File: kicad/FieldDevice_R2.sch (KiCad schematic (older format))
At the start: 0 parts

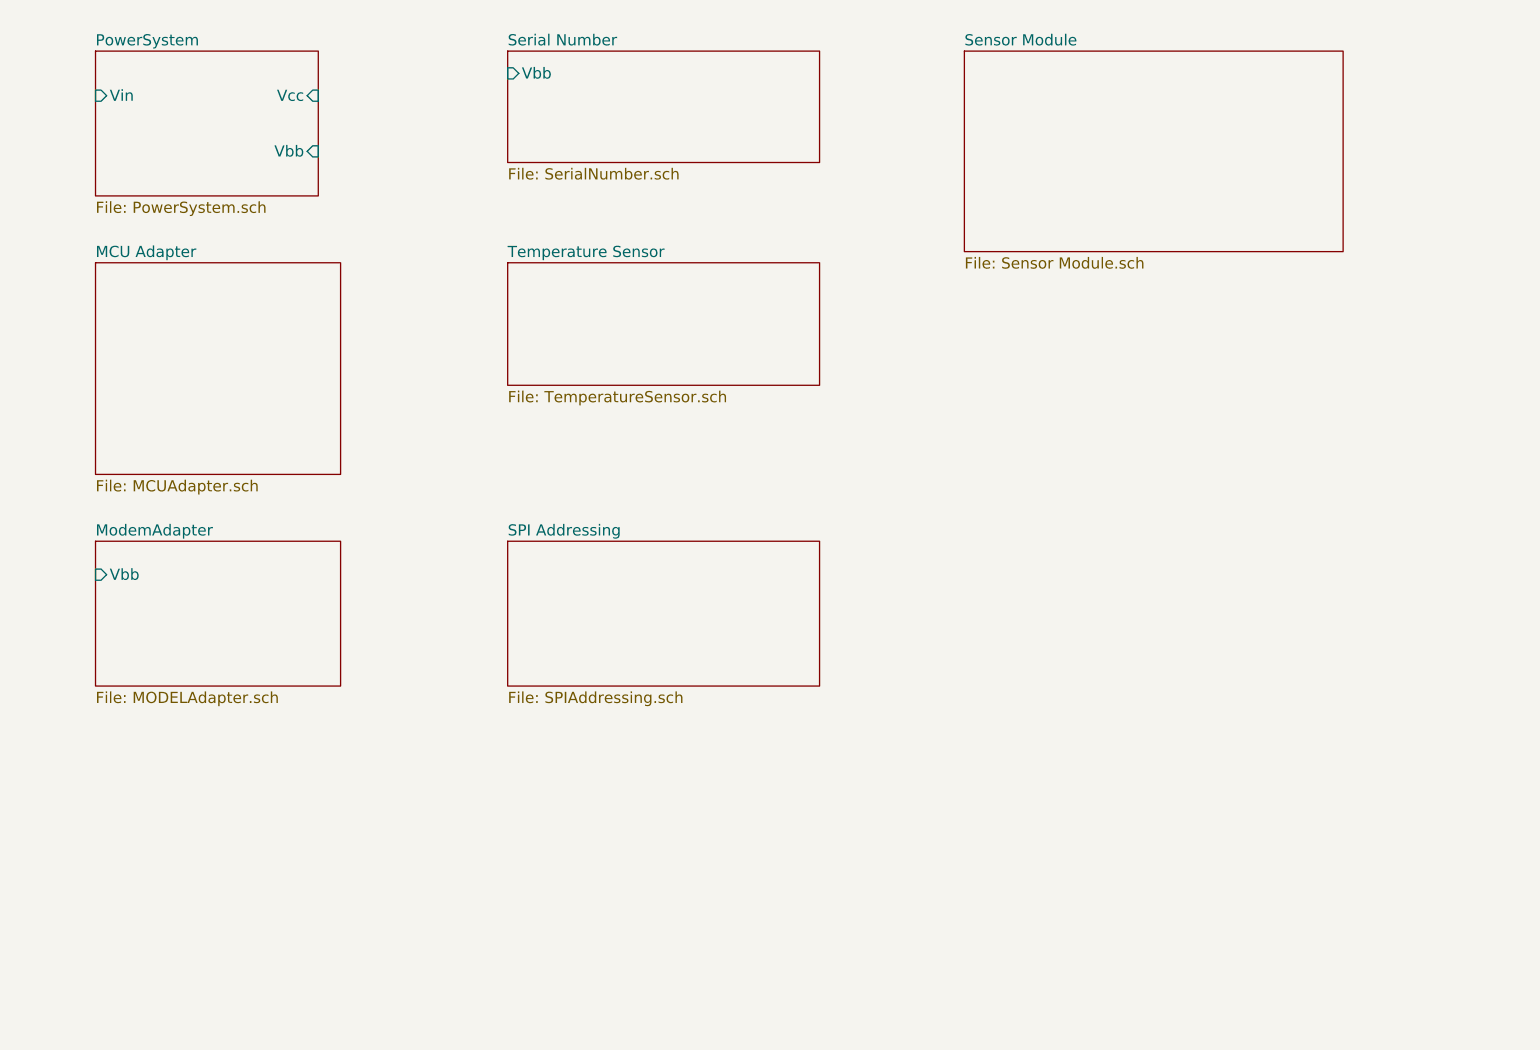
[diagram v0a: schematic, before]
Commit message: First draft of some of the sub-sheets
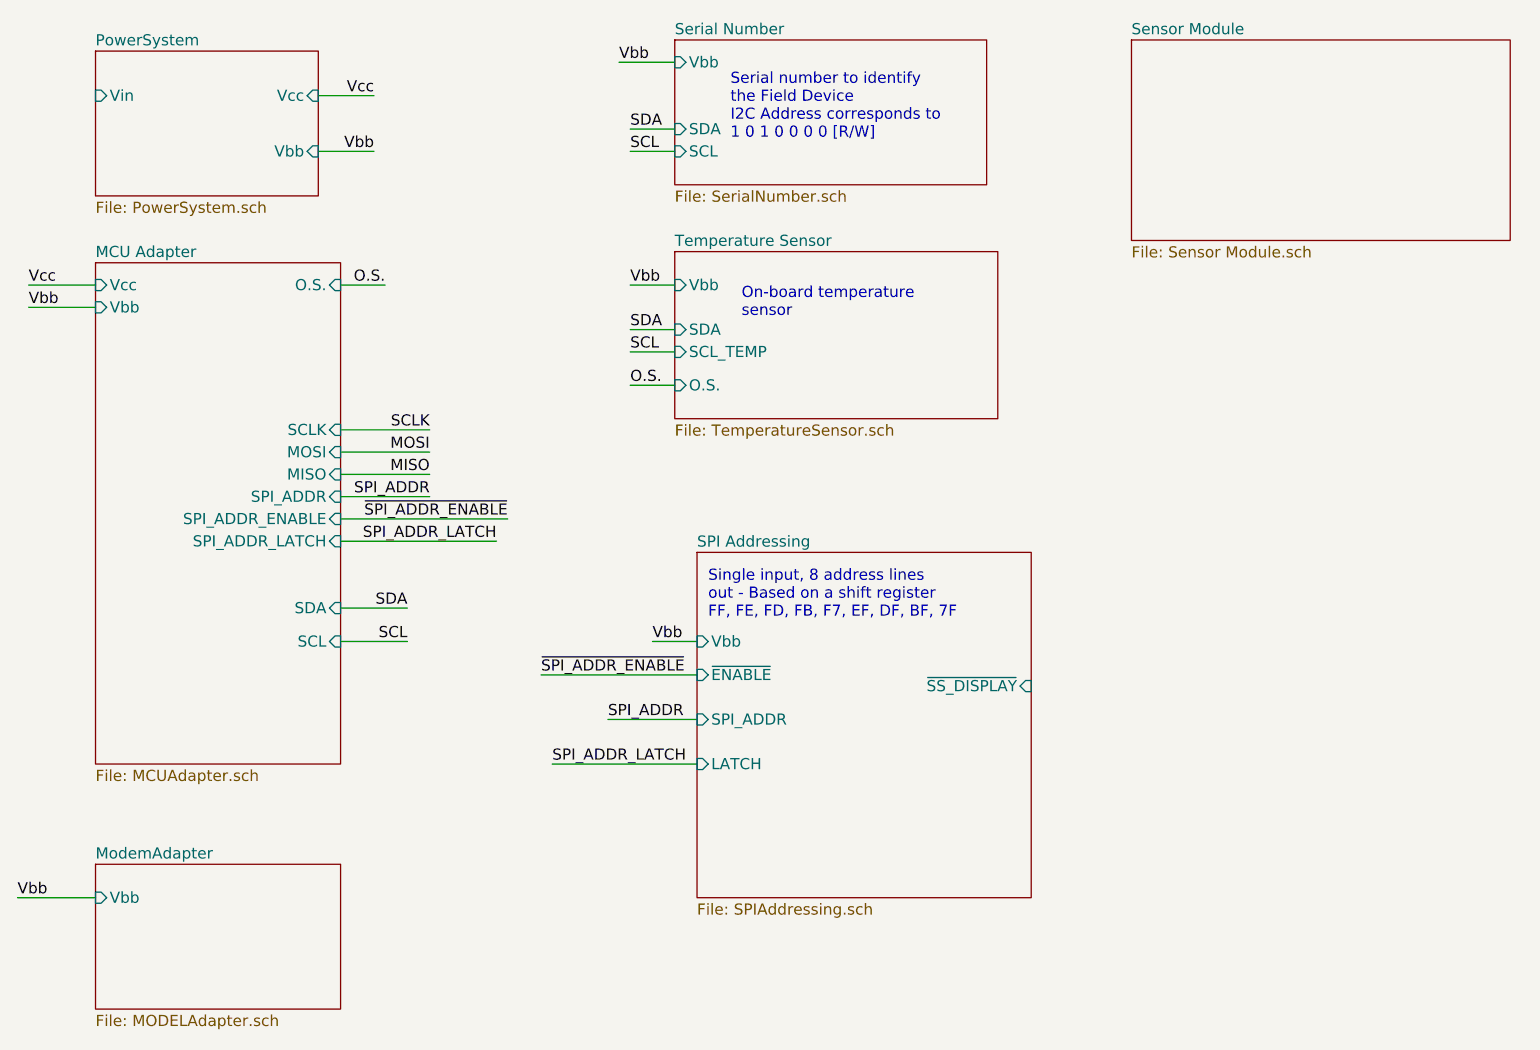
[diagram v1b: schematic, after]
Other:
- note added: "On-board temperature \nsensor"
- note added: "Serial number to identify \nthe Field Device\nI2C Address corresponds to \n1 0 1 0 0 0 0 [R/W]"
- note added: "Single input, 8 address lines \nout - Based on a shift register\nFF, FE, FD, FB, F7, EF, DF, BF, 7F"
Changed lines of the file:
@@
 EESchema Schematic File Version 4
 LIBS:FieldDevice_R2-cache
+LIBS:FieldDevice_Power_5V-cache
 EELAYER 26 0
 EELAYER END
@@
 $EndSheet
 $Sheet
-S 3450 3100 1400 650
-U 5C1FCC69
-F0 "SPI Addressing" 50
-F1 "SPIAddressing.sch" 50
-$EndSheet
-$Sheet
-S 3450 900  1400 500
+S 4200 850  1400 650
 U 5C1FCC6C
 F0 "Serial Number" 50
 F1 "SerialNumber.sch" 50
-F2 "Vbb" I L 3450 1000 50
+F2 "Vbb" I L 4200 950 50
+F3 "SDA" I L 4200 1250 50
+F4 "SCL" I L 4200 1350 50
 $EndSheet
 $Sheet
-S 3450 1850 1400 550
+S 4200 1800 1450 750
 U 5C1FCC6F
 F0 "Temperature Sensor" 50
 F1 "TemperatureSensor.sch" 50
+F2 "O.S." I L 4200 2400 50
+F3 "SCL_TEMP" I L 4200 2250 50
+F4 "SDA" I L 4200 2150 50
+F5 "Vbb" I L 4200 1950 50
 $EndSheet
 $Sheet
-S 5500 900  1700 900
+S 6250 850  1700 900
 U 5C1FCC72
 F0 "Sensor Module" 50
@@
 $EndSheet
 $Sheet
-S 1600 1850 1100 950
+S 1600 1850 1100 2250
 U 5C1FCC75
 F0 "MCU Adapter" 50
 F1 "MCUAdapter.sch" 50
+F2 "Vcc" I L 1600 1950 50
+F3 "Vbb" I L 1600 2050 50
+F4 "SDA" I R 2700 3400 50
+F5 "SCL" I R 2700 3550 50
+F6 "O.S." I R 2700 1950 50
+F7 "SPI_ADDR" I R 2700 2900 50
+F8 "SCLK" I R 2700 2600 50
+F9 "MOSI" I R 2700 2700 50
+F10 "MISO" I R 2700 2800 50
+F11 "SPI_ADDR_ENABLE" I R 2700 3000 50
+F12 "SPI_ADDR_LATCH" I R 2700 3100 50
 $EndSheet
 $Sheet
-S 1600 3100 1100 650
+S 1600 4550 1100 650
 U 5C1FCC78
 F0 "ModemAdapter" 50
 F1 "MODELAdapter.sch" 50
-F2 "Vbb" I L 1600 3250 50
+F2 "Vbb" I L 1600 4700 50
 $EndSheet
+Text Notes 4350 3450 0    50   ~ 0
+Single input, 8 address lines \nout - Based on a shift register\nFF, FE, FD, FB, F7, EF, DF, BF, 7F
+Text Notes 4450 1300 0    50   ~ 0
+Serial number to identify \nthe Field Device\nI2C Address corresponds to \n1 0 1 0 0 0 0 [R/W]
+Text Notes 4500 2100 0    50   ~ 0
+On-board temperature \nsensor
+Wire Wire Line
+	2600 1350 2850 1350
+Text Label 2850 1350 2    50   ~ 0
+Vbb
+Wire Wire Line
+	4200 950  3950 950
+Text Label 3950 950  0    50   ~ 0
+Vbb
+Wire Wire Line
+	4200 1950 4000 1950
+Text Label 4000 1950 0    50   ~ 0
+Vbb
+Wire Wire Line
+	2700 3550 3000 3550
+Wire Wire Line
+	2700 3400 3000 3400
+Text Label 3000 3400 2    50   ~ 0
+SDA
+Wire Wire Line
+	4200 2150 4000 2150
+Text Label 4000 2150 0    50   ~ 0
+SDA
+Wire Wire Line
+	4200 2250 4000 2250
+Text Label 4000 2250 0    50   ~ 0
+SCL
+Wire Wire Line
+	4200 2400 4000 2400
+Text Label 4000 2400 0    50   ~ 0
+O.S.
+Wire Wire Line
+	2700 1950 2900 1950
+Text Label 2900 1950 2    50   ~ 0
+O.S.
+Wire Wire Line
+	2600 1100 2850 1100
+Text Label 2850 1100 2    50   ~ 0
+Vcc
+Wire Wire Line
+	1600 1950 1300 1950
+Wire Wire Line
+	1600 2050 1300 2050
+Text Label 1300 1950 0    50   ~ 0
+Vcc
+Text Label 1300 2050 0    50   ~ 0
+Vbb
+Wire Wire Line
+	1600 4700 1250 4700
+Text Label 1250 4700 0    50   ~ 0
+Vbb
+Wire Wire Line
+	4300 3550 4100 3550
+Text Label 4100 3550 0    50   ~ 0
+Vbb
+Wire Wire Line
+	4200 1250 4000 1250
+Wire Wire Line
+	4200 1350 4000 1350
+Text Label 3000 3550 2    50   ~ 0
+SCL
+$Sheet
+S 4300 3150 1500 1550
+U 5C1FCC69
+F0 "SPI Addressing" 50
+F1 "SPIAddressing.sch" 50
+F2 "Vbb" I L 4300 3550 50
+F3 "SPI_ADDR" I L 4300 3900 50
+F4 "~SS_DISPLAY" I R 5800 3750 50
+F5 "LATCH" I L 4300 4100 50
+F6 "~ENABLE" I L 4300 3700 50
+$EndSheet
+Text Label 4000 1250 0    50   ~ 0
+SDA
+Text Label 4000 1350 0    50   ~ 0
+SCL
+Text Label 3900 3900 0    50   ~ 0
+SPI_ADDR
+Wire Wire Line
+	4300 3900 3900 3900
+Wire Wire Line
+	2700 2900 3100 2900
+Text Label 3100 2900 2    50   ~ 0
+SPI_ADDR
+Wire Wire Line
+	2700 2800 3100 2800
+Wire Wire Line
+	2700 2700 3100 2700
+Wire Wire Line
+	2700 2600 3100 2600
+Text Label 3100 2600 2    50   ~ 0
+SCLK
+Text Label 3100 2700 2    50   ~ 0
+MOSI
+Text Label 3100 2800 2    50   ~ 0
+MISO
+Text Label 3600 3700 0    50   ~ 0
+~SPI_ADDR_ENABLE
+Wire Wire Line
+	4300 3700 3600 3700
+Wire Wire Line
+	2700 3000 3450 3000
+Text Label 3450 3000 2    50   ~ 0
+~SPI_ADDR_ENABLE
+Text Label 3650 4100 0    50   ~ 0
+SPI_ADDR_LATCH
+Wire Wire Line
+	4300 4100 3650 4100
+Text Label 3400 3100 2    50   ~ 0
+SPI_ADDR_LATCH
+Wire Wire Line
+	2700 3100 3400 3100
 $EndSCHEMATC

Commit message: Added some more detail and moved the display from SPI to I2C
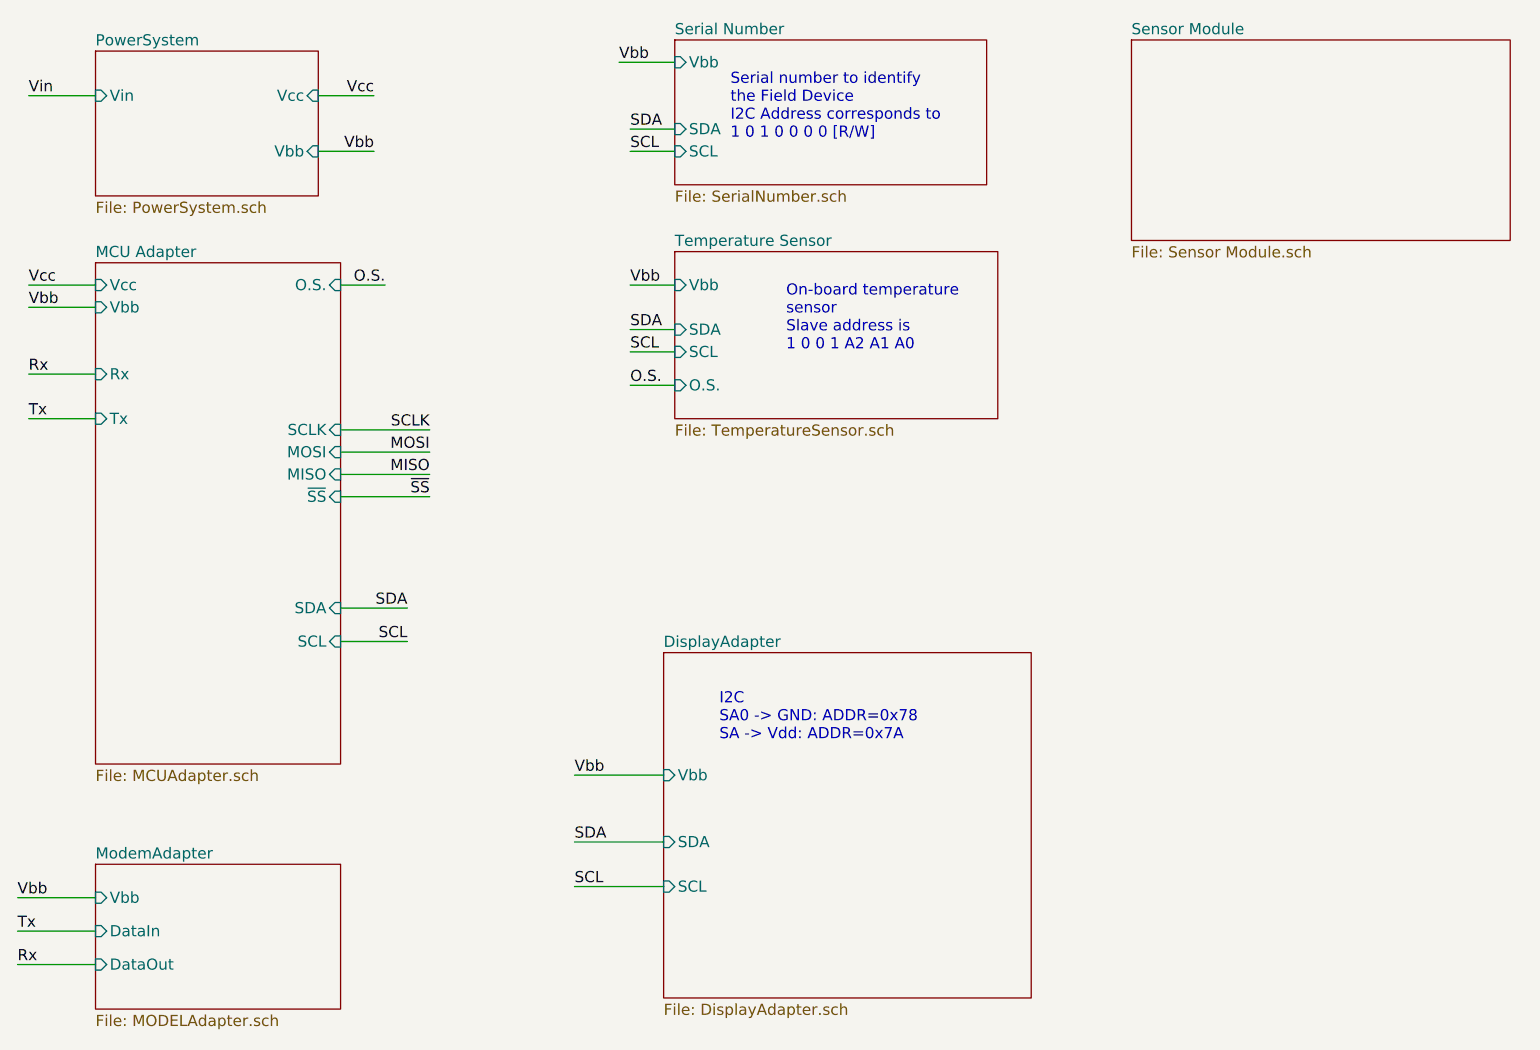
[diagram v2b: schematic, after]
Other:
- note added: "I2C \nSA0 -> GND: ADDR=0x78\nSA -> Vdd: ADDR=0x7A"
- note added: "On-board temperature \nsensor\nSlave address is \n1 0 0 1 A2 A1 A0"
- note removed: "On-board temperature \nsensor"
- note removed: "Single input, 8 address lines \nout - Based on a shift register\nFF, FE, FD, FB, F7, EF, DF, BF, 7F"
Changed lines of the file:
@@
 EESchema Schematic File Version 4
 LIBS:FieldDevice_R2-cache
-LIBS:FieldDevice_Power_5V-cache
-EELAYER 26 0
+EELAYER 29 0
 EELAYER END
-$Descr A4 11693 8268
+$Descr A3 16535 11693
 encoding utf-8
 Sheet 1 8
@@
 F1 "TemperatureSensor.sch" 50
 F2 "O.S." I L 4200 2400 50
-F3 "SCL_TEMP" I L 4200 2250 50
+F3 "SCL" I L 4200 2250 50
 F4 "SDA" I L 4200 2150 50
 F5 "Vbb" I L 4200 1950 50
@@
 F5 "SCL" I R 2700 3550 50
 F6 "O.S." I R 2700 1950 50
-F7 "SPI_ADDR" I R 2700 2900 50
+F7 "~SS" I R 2700 2900 50
 F8 "SCLK" I R 2700 2600 50
 F9 "MOSI" I R 2700 2700 50
 F10 "MISO" I R 2700 2800 50
-F11 "SPI_ADDR_ENABLE" I R 2700 3000 50
-F12 "SPI_ADDR_LATCH" I R 2700 3100 50
+F11 "Rx" I L 1600 2350 50
+F12 "Tx" I L 1600 2550 50
 $EndSheet
 $Sheet
@@
 F0 "ModemAdapter" 50
 F1 "MODELAdapter.sch" 50
-F2 "Vbb" I L 1600 4700 50
-$EndSheet
-Text Notes 4350 3450 0    50   ~ 0
-Single input, 8 address lines \nout - Based on a shift register\nFF, FE, FD, FB, F7, EF, DF, BF, 7F
+F2 "DataIn" I L 1600 4850 50
+F3 "DataOut" I L 1600 5000 50
+F4 "Vbb" I L 1600 4700 50
+$EndSheet
 Text Notes 4450 1300 0    50   ~ 0
 Serial number to identify \nthe Field Device\nI2C Address corresponds to \n1 0 1 0 0 0 0 [R/W]
-Text Notes 4500 2100 0    50   ~ 0
-On-board temperature \nsensor
+Text Notes 4700 2250 0    50   ~ 0
+On-board temperature \nsensor\nSlave address is \n1 0 0 1 A2 A1 A0
 Wire Wire Line
 	2600 1350 2850 1350
@@
 Vbb
 Wire Wire Line
-	4300 3550 4100 3550
-Text Label 4100 3550 0    50   ~ 0
-Vbb
-Wire Wire Line
 	4200 1250 4000 1250
 Wire Wire Line
@@
 Text Label 3000 3550 2    50   ~ 0
 SCL
-$Sheet
-S 4300 3150 1500 1550
-U 5C1FCC69
-F0 "SPI Addressing" 50
-F1 "SPIAddressing.sch" 50
-F2 "Vbb" I L 4300 3550 50
-F3 "SPI_ADDR" I L 4300 3900 50
-F4 "~SS_DISPLAY" I R 5800 3750 50
-F5 "LATCH" I L 4300 4100 50
-F6 "~ENABLE" I L 4300 3700 50
-$EndSheet
 Text Label 4000 1250 0    50   ~ 0
 SDA
 Text Label 4000 1350 0    50   ~ 0
 SCL
-Text Label 3900 3900 0    50   ~ 0
-SPI_ADDR
-Wire Wire Line
-	4300 3900 3900 3900
 Wire Wire Line
 	2700 2900 3100 2900
 Text Label 3100 2900 2    50   ~ 0
-SPI_ADDR
+~SS
 Wire Wire Line
 	2700 2800 3100 2800
@@
 Text Label 3100 2800 2    50   ~ 0
 MISO
-Text Label 3600 3700 0    50   ~ 0
-~SPI_ADDR_ENABLE
-Wire Wire Line
-	4300 3700 3600 3700
-Wire Wire Line
-	2700 3000 3450 3000
-Text Label 3450 3000 2    50   ~ 0
-~SPI_ADDR_ENABLE
-Text Label 3650 4100 0    50   ~ 0
-SPI_ADDR_LATCH
-Wire Wire Line
-	4300 4100 3650 4100
-Text Label 3400 3100 2    50   ~ 0
-SPI_ADDR_LATCH
-Wire Wire Line
-	2700 3100 3400 3100
+Wire Wire Line
+	1600 1100 1300 1100
+Text Label 1300 1100 0    50   ~ 0
+Vin
+Wire Wire Line
+	1600 4850 1250 4850
+Wire Wire Line
+	1600 5000 1250 5000
+Wire Wire Line
+	1600 2350 1300 2350
+Wire Wire Line
+	1600 2550 1300 2550
+Text Label 1300 2550 0    50   ~ 0
+Tx
+Text Label 1300 2350 0    50   ~ 0
+Rx
+Text Label 1250 5000 0    50   ~ 0
+Rx
+Text Label 1250 4850 0    50   ~ 0
+Tx
+Wire Wire Line
+	3750 4150 4150 4150
+Wire Wire Line
+	4150 4450 3750 4450
+Wire Wire Line
+	4150 4650 3750 4650
+Text Notes 4400 4000 0    50   ~ 0
+I2C \nSA0 -> GND: ADDR=0x78\nSA -> Vdd: ADDR=0x7A
+$Sheet
+S 4150 3600 1650 1550
+U 5CBF851C
+F0 "DisplayAdapter" 50
+F1 "DisplayAdapter.sch" 50
+F2 "SDA" I L 4150 4450 50
+F3 "SCL" I L 4150 4650 50
+F4 "Vbb" I L 4150 4150 50
+$EndSheet
+Text Label 3750 4150 0    50   ~ 0
+Vbb
+Text Label 3750 4450 0    50   ~ 0
+SDA
+Text Label 3750 4650 0    50   ~ 0
+SCL
 $EndSCHEMATC

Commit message: Revision 3
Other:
- note added: "DISPLAY"
- note added: "EA DOGS104-A\nEA LED36X28-A Amber Backlight"
- note added: "I2C"
- note added: "I2C \nSA0 -> GND: ADDR=0x78 ***\nSA0 -> Vdd: ADDR=0x7A"
- note added: "SPI"
- note added: "USART"
- note removed: "I2C \nSA0 -> GND: ADDR=0x78\nSA -> Vdd: ADDR=0x7A"
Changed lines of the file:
@@
 F2 "Vcc" I L 1600 1950 50
 F3 "Vbb" I L 1600 2050 50
-F4 "SDA" I R 2700 3400 50
-F5 "SCL" I R 2700 3550 50
+F4 "SDA" I R 2700 3150 50
+F5 "SCL" I R 2700 3300 50
 F6 "O.S." I R 2700 1950 50
 F7 "~SS" I R 2700 2900 50
@@
 F11 "Rx" I L 1600 2350 50
 F12 "Tx" I L 1600 2550 50
+F13 "DISP_BACKLIGHT" I R 2700 3700 50
+F14 "~DISP_RESET" I R 2700 3900 50
 $EndSheet
 $Sheet
@@
 F0 "ModemAdapter" 50
 F1 "MODELAdapter.sch" 50
-F2 "DataIn" I L 1600 4850 50
-F3 "DataOut" I L 1600 5000 50
-F4 "Vbb" I L 1600 4700 50
+F2 "Vbb" I L 1600 4700 50
+F3 "Rx" I L 1600 5000 50
+F4 "Tx" I L 1600 4850 50
 $EndSheet
 Text Notes 4450 1300 0    50   ~ 0
@@
 Vbb
 Wire Wire Line
-	2700 3550 3000 3550
+	2700 3300 3000 3300
 Wire Wire Line
-	2700 3400 3000 3400
-Text Label 3000 3400 2    50   ~ 0
+	2700 3150 3000 3150
+Text Label 3000 3150 2    50   ~ 0
 SDA
 Wire Wire Line
@@
 Wire Wire Line
 	4200 1350 4000 1350
-Text Label 3000 3550 2    50   ~ 0
+Text Label 3000 3300 2    50   ~ 0
 SCL
 Text Label 4000 1250 0    50   ~ 0
@@
 Tx
 Wire Wire Line
-	3750 4150 4150 4150
+	5550 3550 6250 3550
 Wire Wire Line
-	4150 4450 3750 4450
+	6250 3700 5550 3700
 Wire Wire Line
-	4150 4650 3750 4650
-Text Notes 4400 4000 0    50   ~ 0
-I2C \nSA0 -> GND: ADDR=0x78\nSA -> Vdd: ADDR=0x7A
+	6250 3900 5550 3900
+Text Notes 6700 3500 0    50   ~ 0
+I2C \nSA0 -> GND: ADDR=0x78 ***\nSA0 -> Vdd: ADDR=0x7A
 $Sheet
-S 4150 3600 1650 1550
+S 6250 3200 1650 1550
 U 5CBF851C
 F0 "DisplayAdapter" 50
 F1 "DisplayAdapter.sch" 50
-F2 "SDA" I L 4150 4450 50
-F3 "SCL" I L 4150 4650 50
-F4 "Vbb" I L 4150 4150 50
+F2 "SDA" I L 6250 3700 50
+F3 "SCL" I L 6250 3900 50
+F4 "Vbb" I L 6250 3550 50
+F5 "~RESET" I L 6250 4400 50
+F6 "BACKLIGHT" I L 6250 4150 50
 $EndSheet
-Text Label 3750 4150 0    50   ~ 0
+Text Label 5550 3550 0    50   ~ 0
 Vbb
-Text Label 3750 4450 0    50   ~ 0
+Text Label 5550 3700 0    50   ~ 0
 SDA
-Text Label 3750 4650 0    50   ~ 0
+Text Label 5550 3900 0    50   ~ 0
 SCL
+Wire Wire Line
+	6250 4150 5550 4150
+Wire Wire Line
+	6250 4400 5550 4400
+Text Label 5550 4150 0    50   ~ 0
+DISP_BACKLIGHT
+Text Label 5550 4400 0    50   ~ 0
+~DISP_RESET
+Text Notes 6500 4700 0    50   ~ 0
+EA DOGS104-A\nEA LED36X28-A Amber Backlight
+Wire Wire Line
+	2700 3700 3400 3700
+Wire Wire Line
+	2700 3900 3400 3900
+Text Label 3400 3700 2    50   ~ 0
+DISP_BACKLIGHT
+Text Label 3400 3900 2    50   ~ 0
+~DISP_RESET
+Text Notes 1900 2550 1    50   ~ 0
+USART
+Text Notes 2400 2750 1    50   ~ 0
+SPI
+Text Notes 2400 3300 1    50   ~ 0
+I2C
+Text Notes 1950 3950 1    50   ~ 0
+DISPLAY
 $EndSCHEMATC
